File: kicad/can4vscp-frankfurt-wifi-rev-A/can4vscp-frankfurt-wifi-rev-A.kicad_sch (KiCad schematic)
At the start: 13 parts, among them J2 Conn_01x04_Male, U1 ESP32-WROOM-32, U2 SN65HVD233

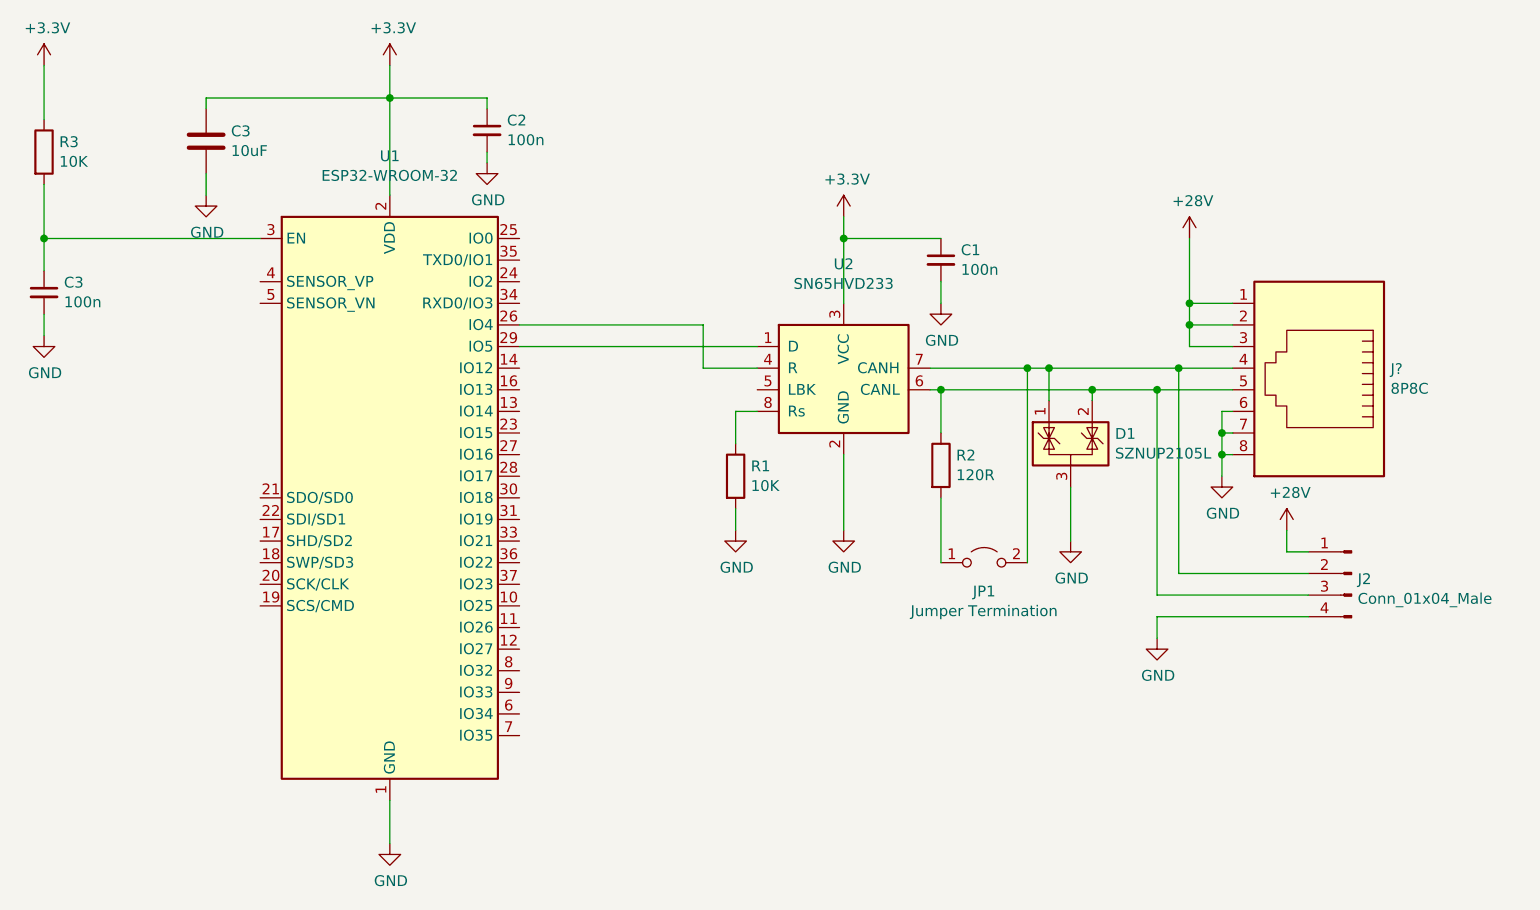
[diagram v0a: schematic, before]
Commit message: Updated to KiCad 9
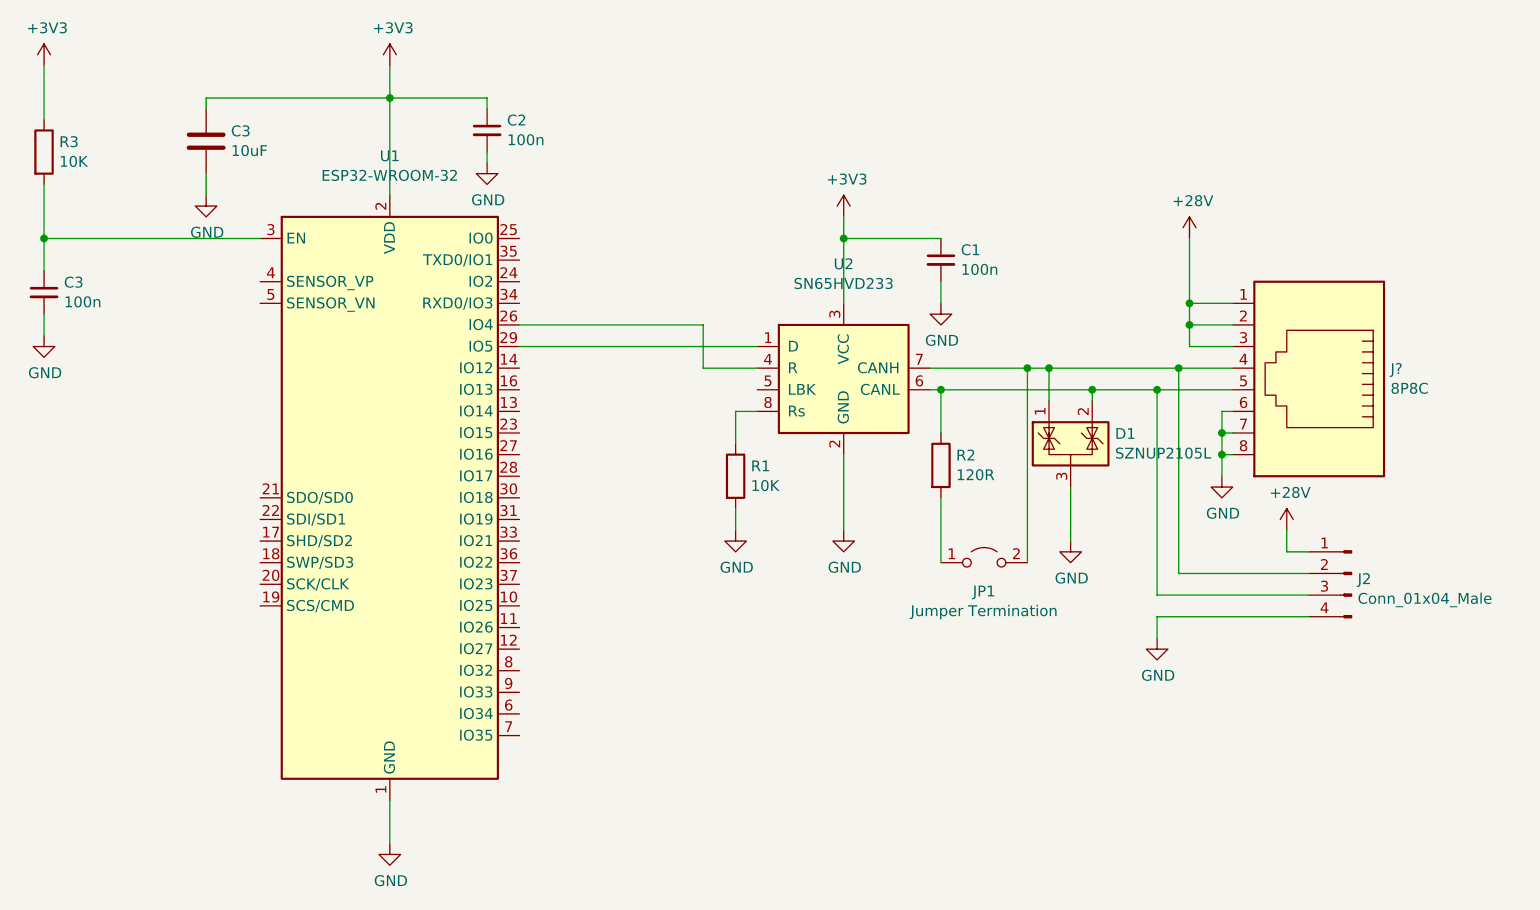
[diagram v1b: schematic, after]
